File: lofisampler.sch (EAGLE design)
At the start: 60 parts, among them IC1 ISD1820, IC2 78L05Z, IC3 LM358N

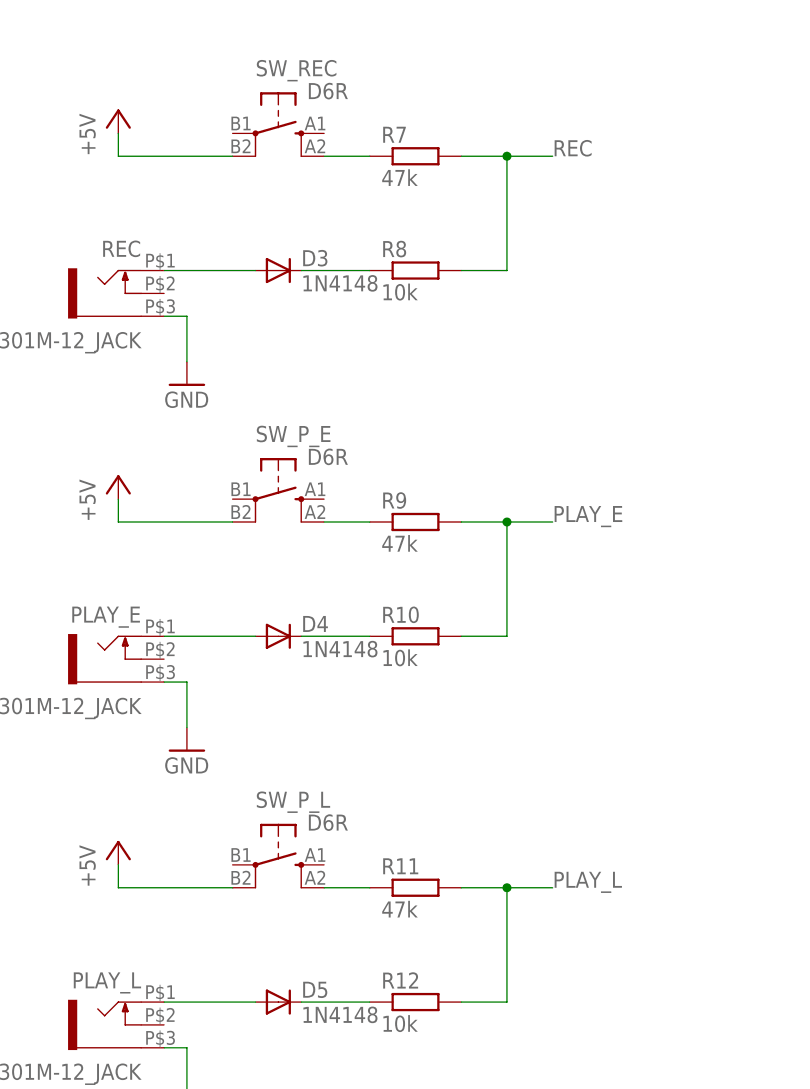
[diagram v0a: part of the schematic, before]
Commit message: Changed current limit resistors for the push buttons to 10k. Using 47k seems to deliver too small a current sometimes (some chips do not trigger on this).
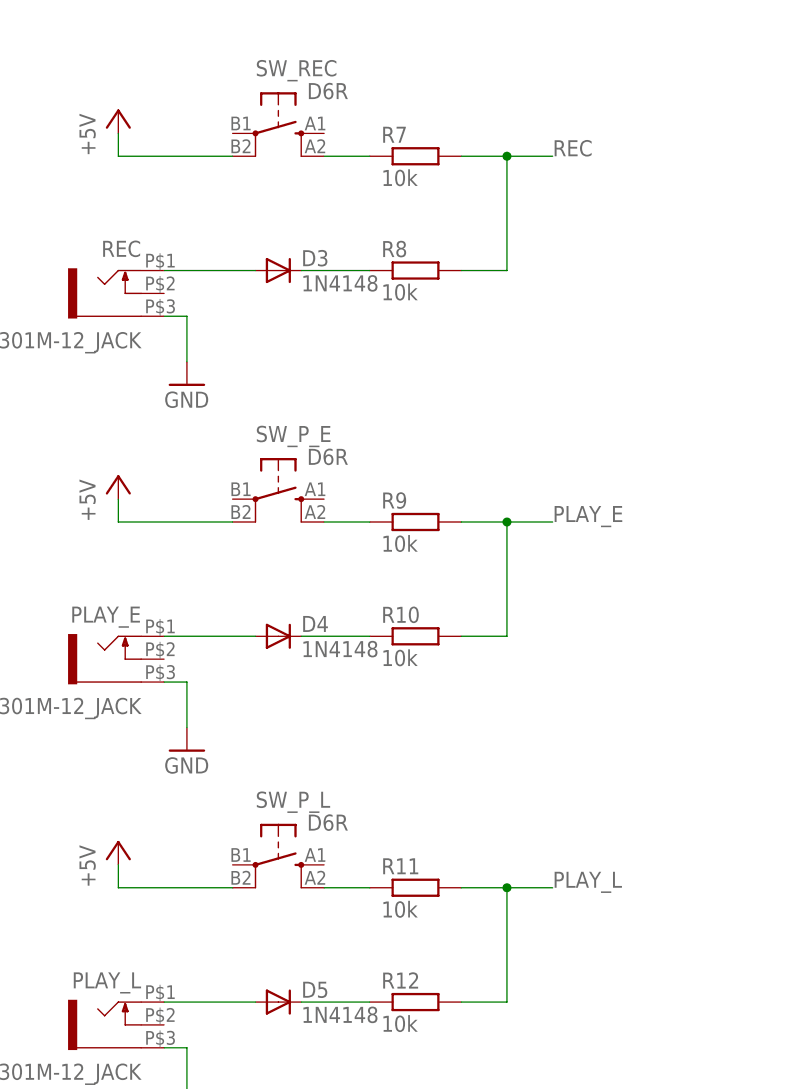
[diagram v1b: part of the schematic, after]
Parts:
- R11, R7, R9: value 47k -> 10k
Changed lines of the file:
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@@
 <?xml version="1.0" encoding="utf-8"?>
 <!DOCTYPE eagle SYSTEM "eagle.dtd">
-<eagle version="8.5.1">
+<eagle version="9.0.1">
 <drawing>
 <settings>
@@
 <part name="REC" library="thonkiconn" deviceset="WQP-PJ301M-12_JACK" device=""/>
 <part name="D3" library="diode" library_urn="urn:adsk.eagle:library:210" deviceset="1N4148" device="DO35-7" package3d_urn="urn:adsk.eagle:package:43339/1" value="1N4148"/>
-<part name="R7" library="rcl" library_urn="urn:adsk.eagle:library:334" deviceset="R-EU_" device="0207/2V" package3d_urn="urn:adsk.eagle:package:23490/1" value="47k"/>
+<part name="R7" library="rcl" library_urn="urn:adsk.eagle:library:334" deviceset="R-EU_" device="0207/2V" package3d_urn="urn:adsk.eagle:package:23490/1" value="10k"/>
 <part name="R8" library="rcl" library_urn="urn:adsk.eagle:library:334" deviceset="R-EU_" device="0207/2V" package3d_urn="urn:adsk.eagle:package:23490/1" value="10k"/>
 <part name="P+8" library="supply1" library_urn="urn:adsk.eagle:library:371" deviceset="+5V" device=""/>
@@
 <part name="PLAY_E" library="thonkiconn" deviceset="WQP-PJ301M-12_JACK" device=""/>
 <part name="D4" library="diode" library_urn="urn:adsk.eagle:library:210" deviceset="1N4148" device="DO35-7" package3d_urn="urn:adsk.eagle:package:43339/1" value="1N4148"/>
-<part name="R9" library="rcl" library_urn="urn:adsk.eagle:library:334" deviceset="R-EU_" device="0207/2V" package3d_urn="urn:adsk.eagle:package:23490/1" value="47k"/>
+<part name="R9" library="rcl" library_urn="urn:adsk.eagle:library:334" deviceset="R-EU_" device="0207/2V" package3d_urn="urn:adsk.eagle:package:23490/1" value="10k"/>
 <part name="R10" library="rcl" library_urn="urn:adsk.eagle:library:334" deviceset="R-EU_" device="0207/2V" package3d_urn="urn:adsk.eagle:package:23490/1" value="10k"/>
 <part name="P+9" library="supply1" library_urn="urn:adsk.eagle:library:371" deviceset="+5V" device=""/>
@@
 <part name="PLAY_L" library="thonkiconn" deviceset="WQP-PJ301M-12_JACK" device=""/>
 <part name="D5" library="diode" library_urn="urn:adsk.eagle:library:210" deviceset="1N4148" device="DO35-7" package3d_urn="urn:adsk.eagle:package:43339/1" value="1N4148"/>
-<part name="R11" library="rcl" library_urn="urn:adsk.eagle:library:334" deviceset="R-EU_" device="0207/2V" package3d_urn="urn:adsk.eagle:package:23490/1" value="47k"/>
+<part name="R11" library="rcl" library_urn="urn:adsk.eagle:library:334" deviceset="R-EU_" device="0207/2V" package3d_urn="urn:adsk.eagle:package:23490/1" value="10k"/>
 <part name="R12" library="rcl" library_urn="urn:adsk.eagle:library:334" deviceset="R-EU_" device="0207/2V" package3d_urn="urn:adsk.eagle:package:23490/1" value="10k"/>
 <part name="P+10" library="supply1" library_urn="urn:adsk.eagle:library:371" deviceset="+5V" device=""/>
